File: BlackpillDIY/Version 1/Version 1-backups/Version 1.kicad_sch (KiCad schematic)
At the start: 44 parts, among them J1 Conn_01x08, J2 Conn_01x08, J3 Debug, J4 Left Header, J5 Right Header, J6 Conn_01x05, J7 Conn_01x05, J8 Conn_01x05, J9 Conn_01x08, SW1 Reset Switch, U1 HT-CT62, U2 STM32F411CCUx, U3 SAM-M8Q, U4 LIS2MDL, Y1 LFXTAL062558Reel, Y2 Crystal_GND24

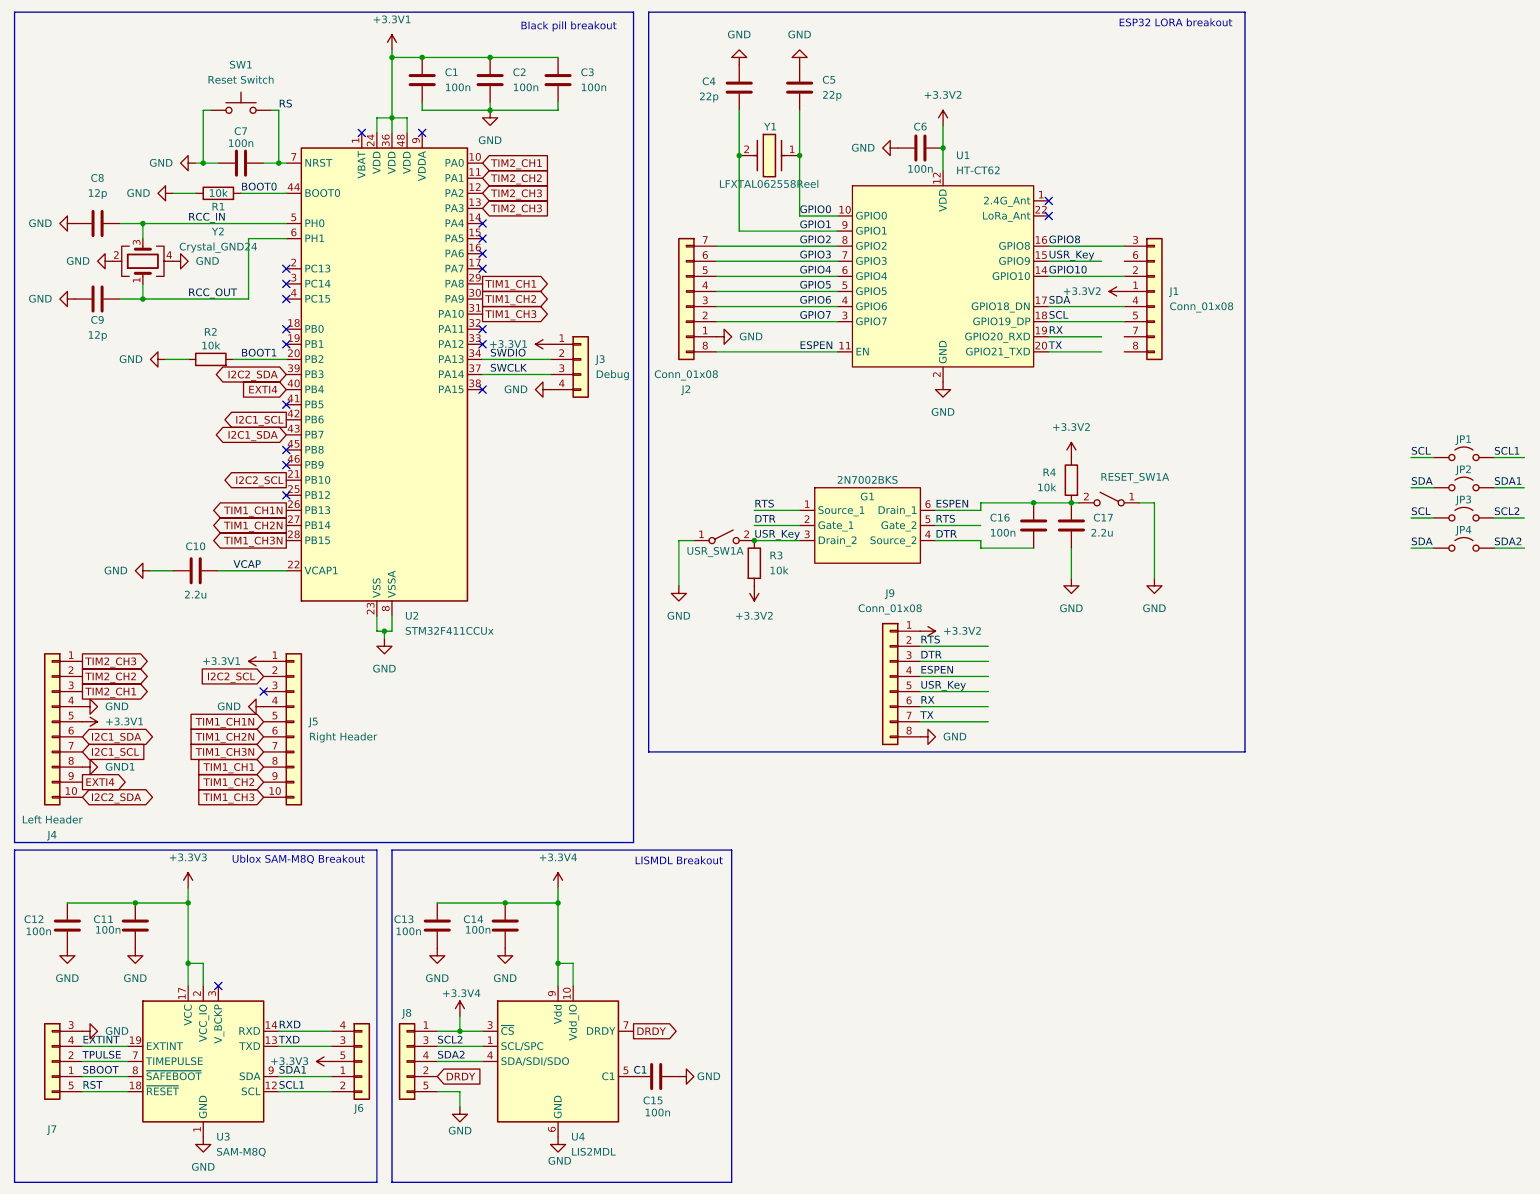
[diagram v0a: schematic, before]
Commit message: Changed to a single breadboard capable PCB
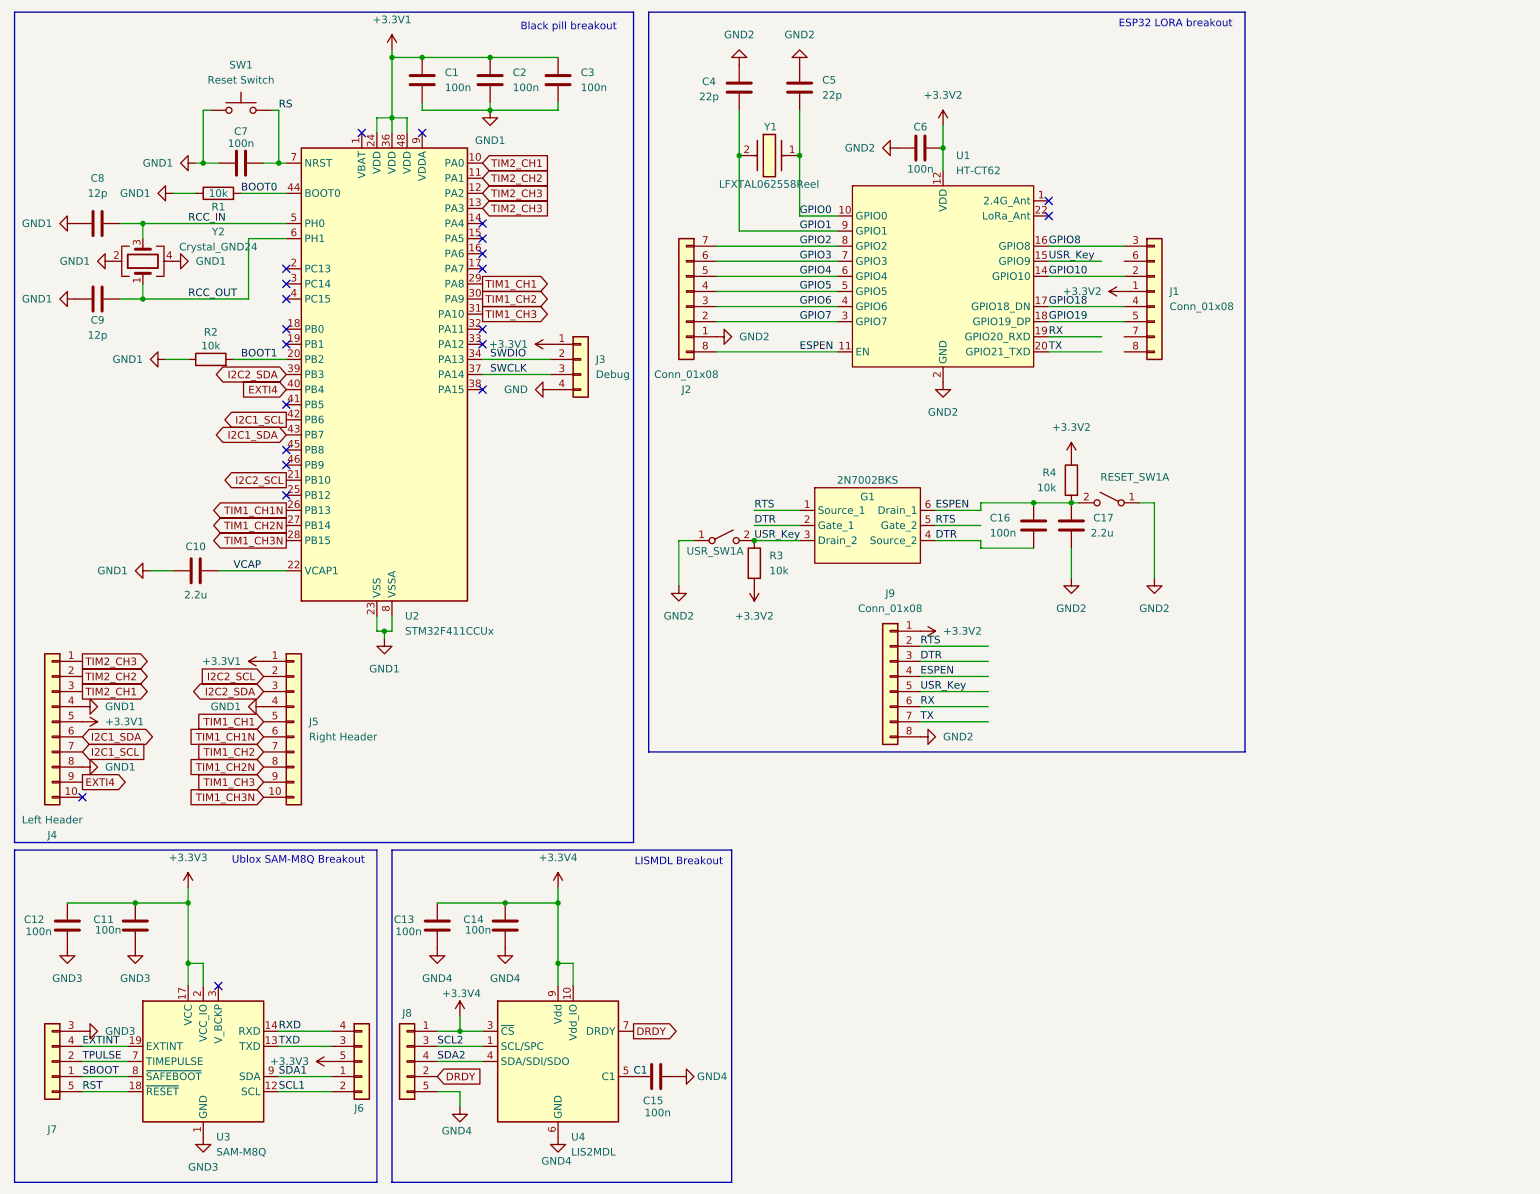
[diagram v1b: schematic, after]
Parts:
- removed JP1, JP2, JP3, JP4: Jumper_2_Open, Connector_PinHeader_2.54mm:PinHeader_1x02_P2.54mm_Vertical, symbol Jumper:Jumper_2_Open
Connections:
- net GND: no longer C1.2, C10.1, C11.2, C12.2, C13.2, C14.2, C15.2, C17.1, C2.2, C3.2, C4.2, C5.2, C6.2, C7.1, C8.1, C9.1, J2.1 (Pin_1), J4.4 (Pin_4), J5.4 (Pin_4), J7.3 (Pin_3), J8.5 (Pin_5), J9.8 (Pin_8), R1.1, R2.1, RESET_SW1.1 (A), SW1.1, U1.13 (GND), U1.2 (GND), U1.21 (GND), U2.23 (VSS), U2.35 (VSS), U2.47 (VSS), U2.49 (VSS), U2.8 (VSSA), U3.1 (GND), U3.10 (GND), U3.11 (GND), U3.15 (GND), U3.16 (GND), U3.20 (GND), U3.4 (GND), U3.5 (GND), U3.6 (GND), U4.6 (GND), U4.8 (GND), USR_SW1.1 (A), Y2.2, Y2.4
- net GND1: now also C1.2, C10.1, C2.2, C3.2, C7.1, C8.1, C9.1, J4.4 (Pin_4), J5.4 (Pin_4), R1.1, R2.1, SW1.1, U2.23 (VSS), U2.35 (VSS), U2.47 (VSS), U2.49 (VSS), U2.8 (VSSA), Y2.2, Y2.4
- net I2C2_SDA: now also J5.3 (Pin_3); no longer J4.10 (Pin_10)
- net TIM1_CH1: now also J5.5 (Pin_5); no longer J5.8 (Pin_8)
- net TIM1_CH1N: now also J5.6 (Pin_6); no longer J5.5 (Pin_5)
- net TIM1_CH2: now also J5.7 (Pin_7); no longer J5.9 (Pin_9)
- net TIM1_CH2N: now also J5.8 (Pin_8); no longer J5.6 (Pin_6)
- net TIM1_CH3: now also J5.9 (Pin_9); no longer J5.10 (Pin_10)
- net TIM1_CH3N: now also J5.10 (Pin_10); no longer J5.7 (Pin_7)
- net SCL renamed GPIO19
- net SDA renamed GPIO18
- new net GND2: C17.1, C4.2, C5.2, C6.2, J2.1 (Pin_1), J9.8 (Pin_8), RESET_SW1.1 (A), U1.13 (GND), U1.2 (GND), U1.21 (GND), USR_SW1.1 (A)
- new net GND3: C11.2, C12.2, J7.3 (Pin_3), U3.1 (GND), U3.10 (GND), U3.11 (GND), U3.15 (GND), U3.16 (GND), U3.20 (GND), U3.4 (GND), U3.5 (GND), U3.6 (GND)
- new net GND4: C13.2, C14.2, C15.2, J8.5 (Pin_5), U4.6 (GND), U4.8 (GND)
